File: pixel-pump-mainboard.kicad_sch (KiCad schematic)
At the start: 113 parts, among them J1 JST NC Valve, J10 BM10B-SRSS-TB(LF)(SN), J11 UART/SWD DNP, J12 TYPE-C-31-M-12, J2 JST NO Valve, J3 6P4C, J4 JST 3 Way Valve, J5 Jack-DC, J6 Phoenix Contact 1733570, J7 BM04B-SRSS-TBT(LF)(SN), J8 SPI, J9 BM04B-SRSS-TBT(LF)(SN), Q1 BSS138, Q2 BSS138, Q3 BSS138, Q4 STN4NF20L, Q5 BSS138, SW1 BOOTSEL, U1 LD1117S33TR, U2 TPS62112RSAR, U3 W25Q128JVS, U4 RP2040, Y1 ABMM2-12.000MHZ-E2-T

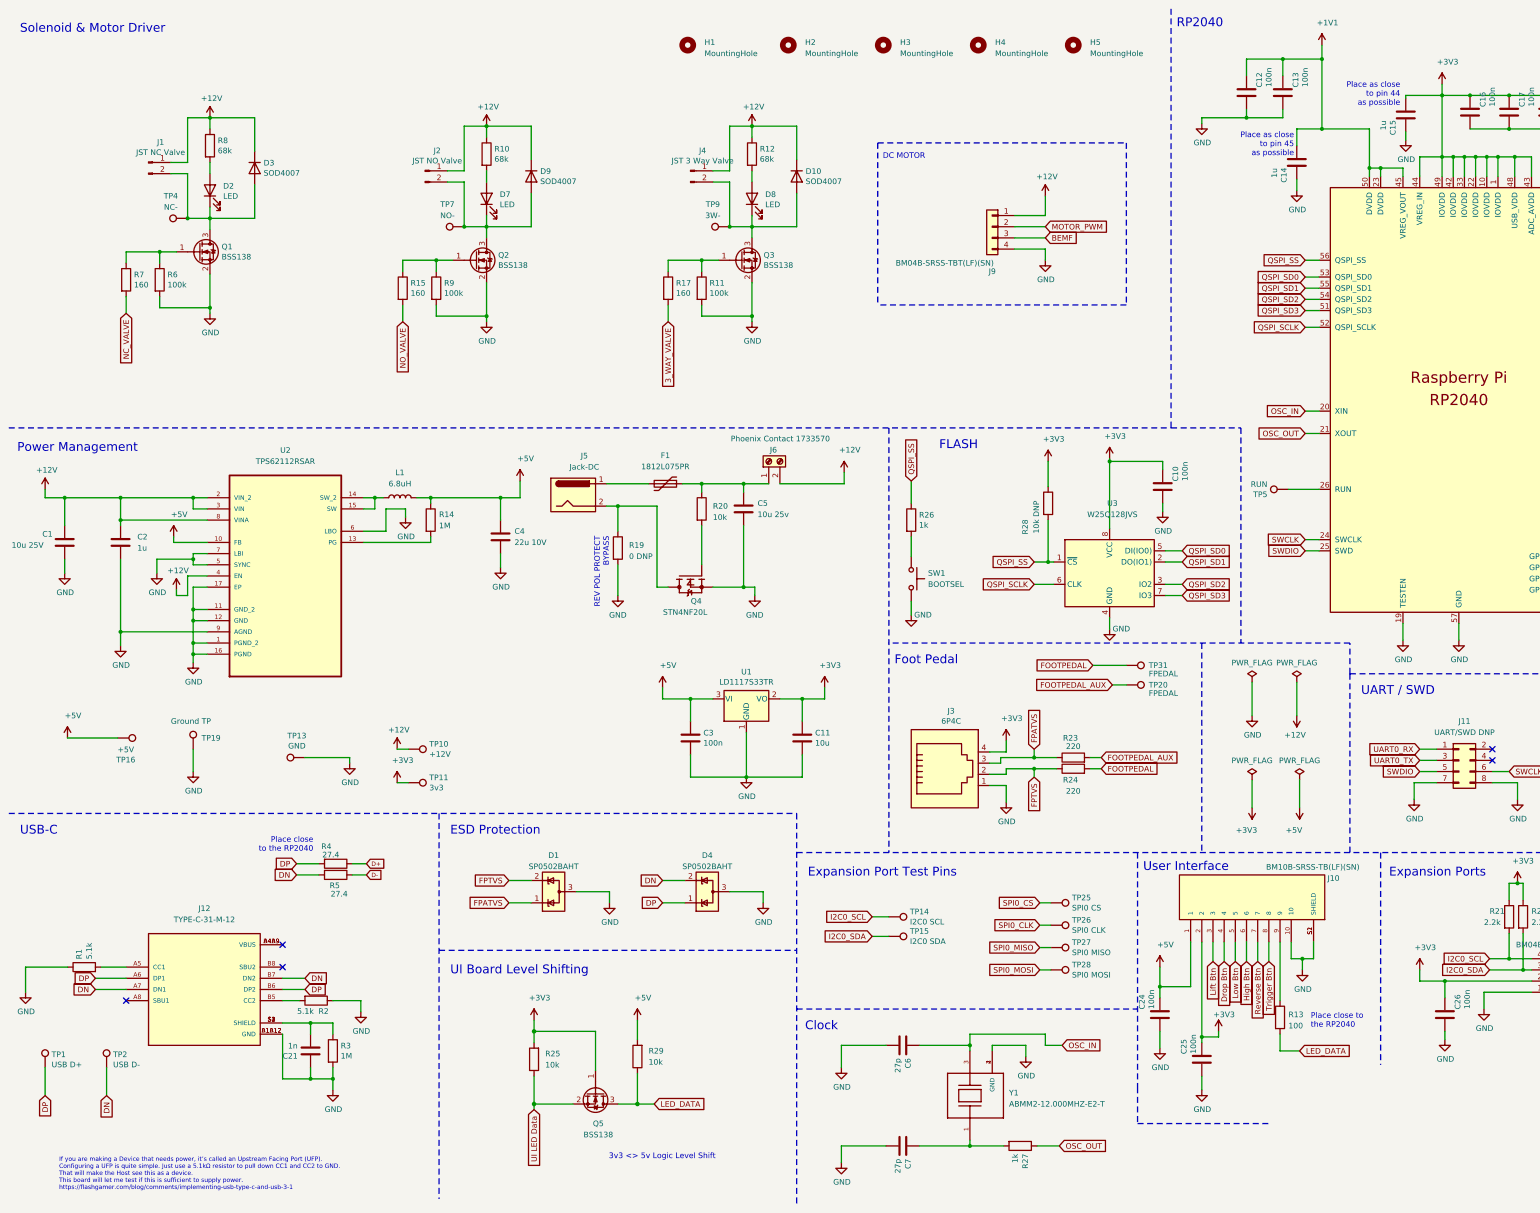
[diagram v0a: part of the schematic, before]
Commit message: Updated schematic for EMI compliance
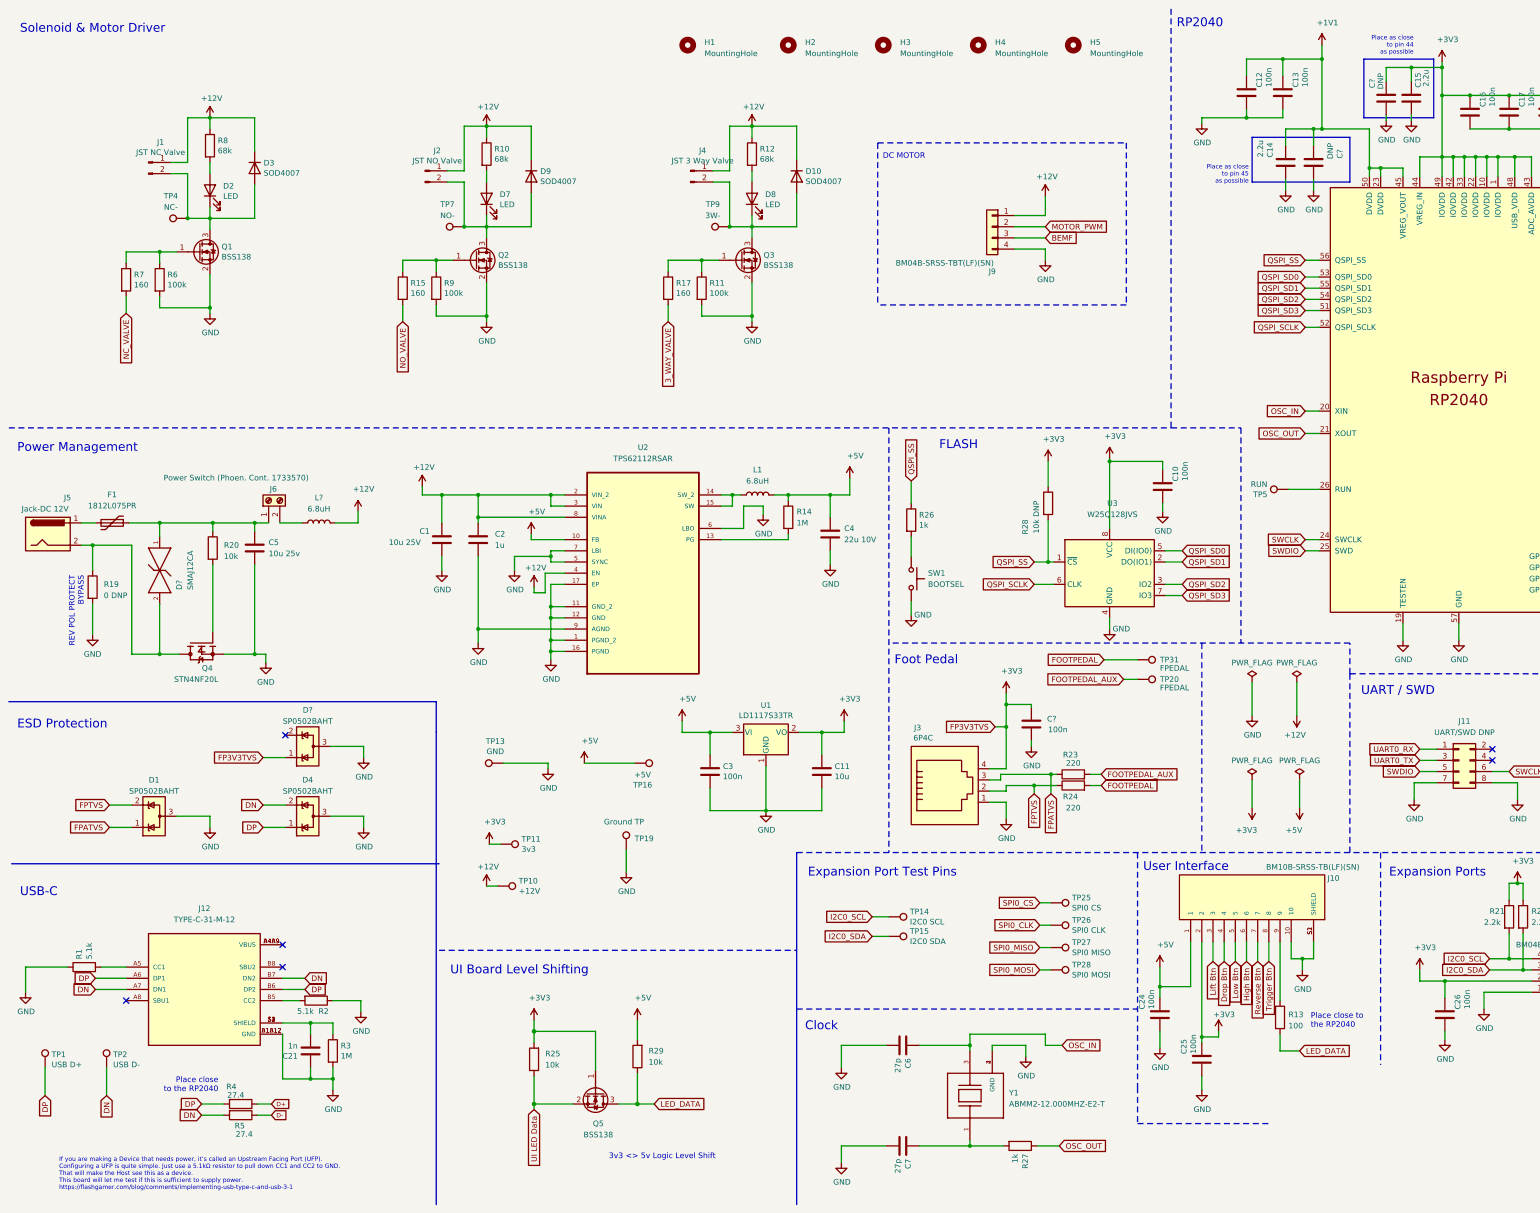
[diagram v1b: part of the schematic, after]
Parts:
- added C?: 100n, Capacitor_SMD:C_0603_1608Metric, symbol Device:C
- added C? (x2): DNP, Capacitor_SMD:C_0402_1005Metric, symbol Device:C
- added D?: SMAJ12CA, Littelfuse_Inc-SMAJ-CA-0-0-*, symbol SMAJ12CA:SMAJ12CA
- added D?: SP0502BAHT, Package_TO_SOT_SMD:SOT-23, symbol Power_Protection:SP0502BAHT
- added L?: 6.8uH, Inductor_SMD:L_TDK_SLF7032, symbol Device:L
- C14, C15: value 1u -> 2.2u
- J5: value Jack-DC -> Jack-DC 12V
- J6: value Phoenix Contact 1733570 -> Power Switch (Phoen. Cont. 1733570)
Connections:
- net +12V: now also L?.2; no longer J6.2 (Pin_2)
- net +1V1: now also C?.1
- net +3V3: now also C?.1, C?.2, D?.1 (K)
- net GND: now also C?.1, C?.2, C?.2, D?.3 (A)
- net at J5.2, Q4.2, Q4.T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: now also D?.2
- net at C5.1, F1.1, J6.1 (Pin_1)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: now also D?.1
- new net: J6.2 (Pin_2), L?.1
- no-connect marks 13 -> 14
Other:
- moved on the sheet: C1, C11, C14, C15, C2, C3, C4, C5, D1, D4, F1, J3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

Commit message: Minor Rev 3 changes
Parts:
- added TP?: PSW2, TestPoint:TestPoint_Pad_D2.0mm, symbol Connector:TestPoint
- added TP?: PSW1, TestPoint:TestPoint_Pad_D2.0mm, symbol Connector:TestPoint
- D2, D7, D8: value LED -> LED DNP
- J6: value Power Switch (Phoen. Cont. 1733570) -> Power Sw
- J7: value BM04B-SRSS-TBT(LF)(SN) -> I2C
- R10, R12, R8: value 68k -> 68k DNP
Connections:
- net at C5.1, D?.1, F1.1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: now also TP?.1
- net at J6.2 (Pin_2), L?.1: now also TP?.1
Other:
- moved on the sheet: D10, D3, D9, J9

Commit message: Minor things fixed
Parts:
- R15, R17, R7: value 160 -> 220
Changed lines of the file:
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@@
       (effects (font (size 1.27 1.27)) (justify left))
     )
-    (property "Value" "160" (id 1) (at 164.338 77.343 0)
+    (property "Value" "220" (id 1) (at 164.338 77.343 0)
       (effects (font (size 1.27 1.27)) (justify left))
     )
@@
       (effects (font (size 1.27 1.27)) (justify left))
     )
-    (property "Value" "160" (id 1) (at 104.013 77.343 0)
+    (property "Value" "220" (id 1) (at 104.013 77.343 0)
       (effects (font (size 1.27 1.27)) (justify left))
     )
@@
       (effects (font (size 1.27 1.27)) (justify left))
     )
-    (property "Value" "160" (id 1) (at 41.148 75.438 0)
+    (property "Value" "220" (id 1) (at 41.148 75.438 0)
       (effects (font (size 1.27 1.27)) (justify left))
     )
@@
     )
     (path "/d4b25396-86cb-4368-ac43-6f12187a3227"
-      (reference "R7") (unit 1) (value "160") (footprint "Resistor_SMD:R_0603_1608Metric")
+      (reference "R7") (unit 1) (value "220") (footprint "Resistor_SMD:R_0603_1608Metric")
     )
     (path "/00000000-0000-0000-0000-000060523731"
@@
     )
     (path "/ce3f1da0-7a25-43f1-9e8d-8d7936ed2f38"
-      (reference "R15") (unit 1) (value "160") (footprint "Resistor_SMD:R_0603_1608Metric")
+      (reference "R15") (unit 1) (value "220") (footprint "Resistor_SMD:R_0603_1608Metric")
     )
     (path "/a4045498-f1c1-4471-ac86-7f541c550939"
-      (reference "R17") (unit 1) (value "160") (footprint "Resistor_SMD:R_0603_1608Metric")
+      (reference "R17") (unit 1) (value "220") (footprint "Resistor_SMD:R_0603_1608Metric")
     )
     (path "/130741ee-b967-45d7-b5e7-3b25dd5ff42c"
